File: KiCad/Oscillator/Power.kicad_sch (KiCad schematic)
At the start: 33 parts, among them SW4 SW_DPST, U10 TL074, U11 TL074, U2 TL074, U3 TL074, U4 40106, U5 TL074, U6 TL074, U7 TL074, U8 TL074, U9 TL074

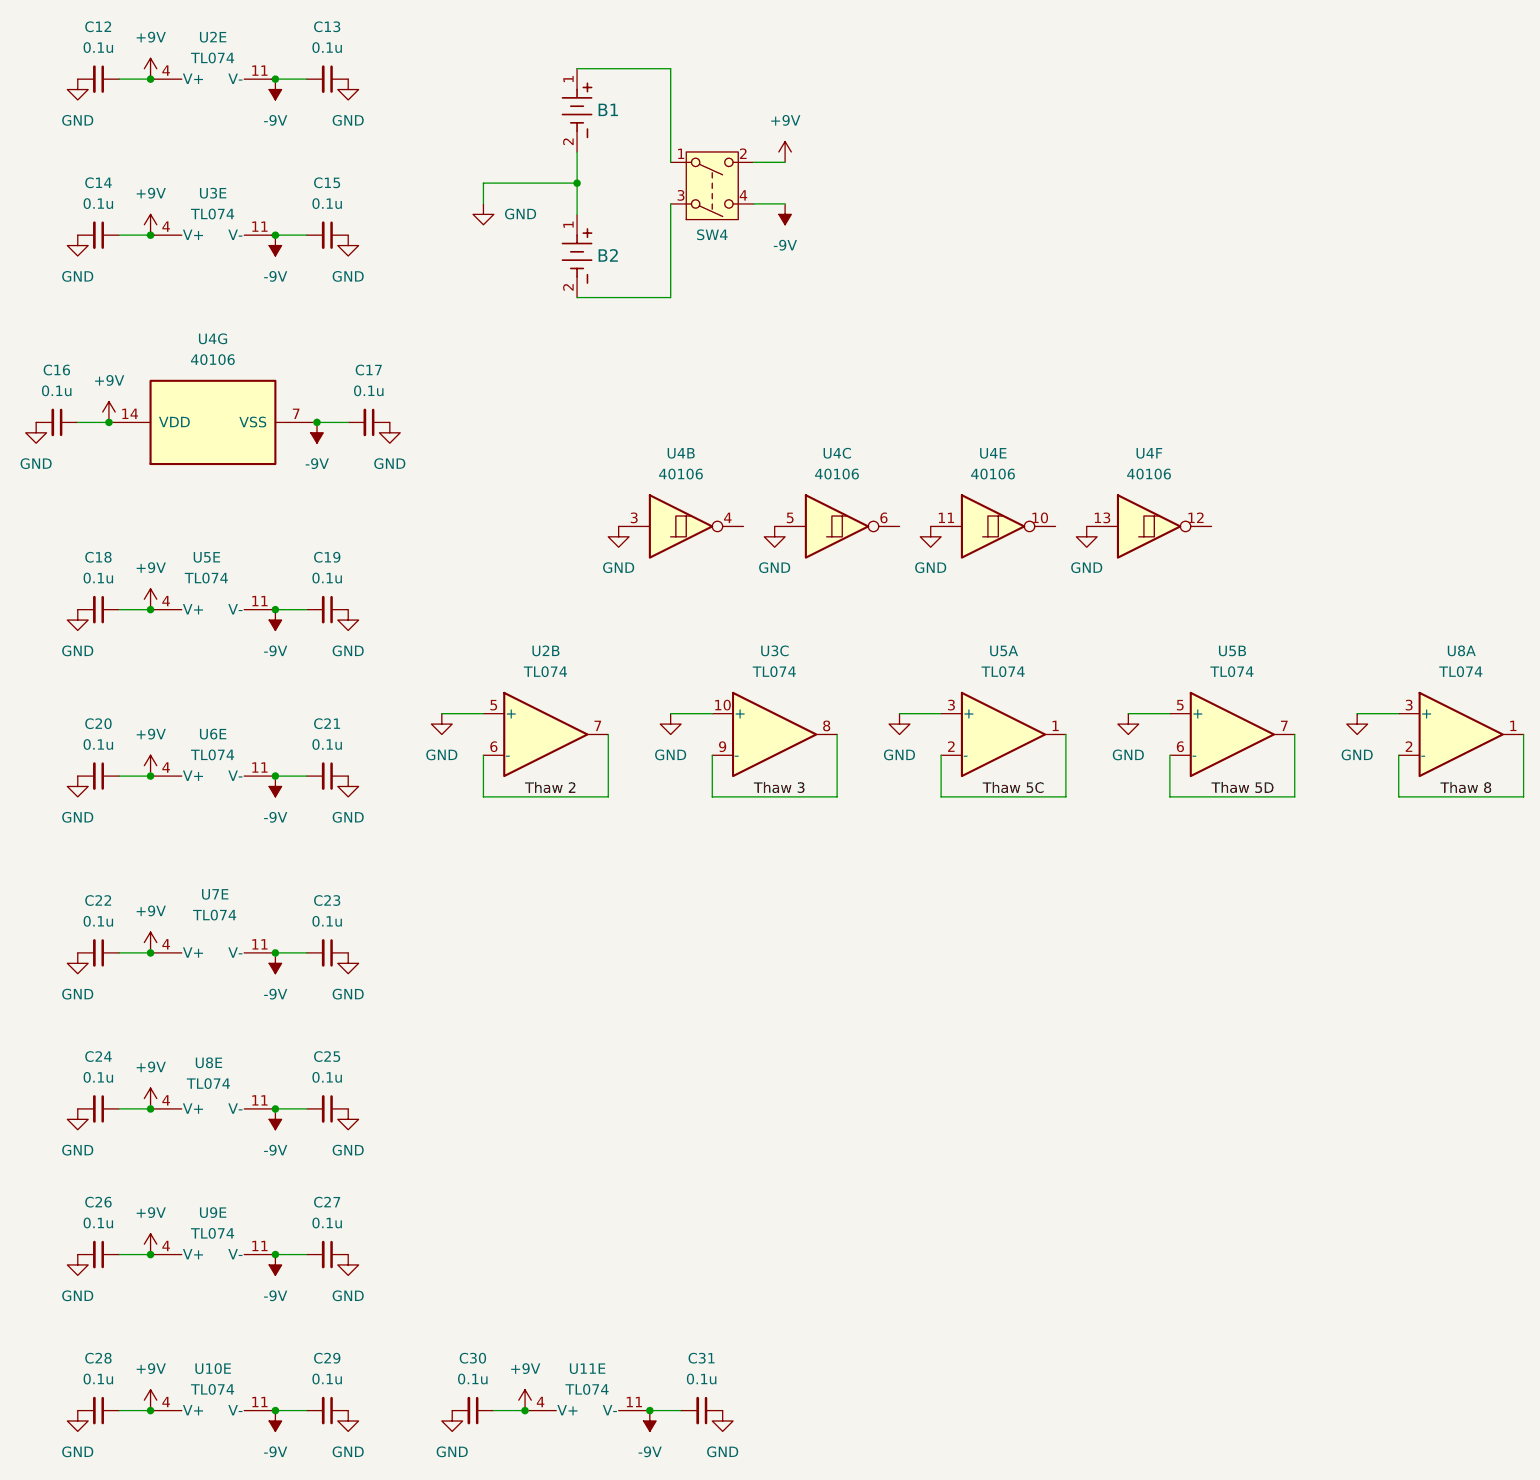
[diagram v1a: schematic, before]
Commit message: finished separating into separate kicad projects
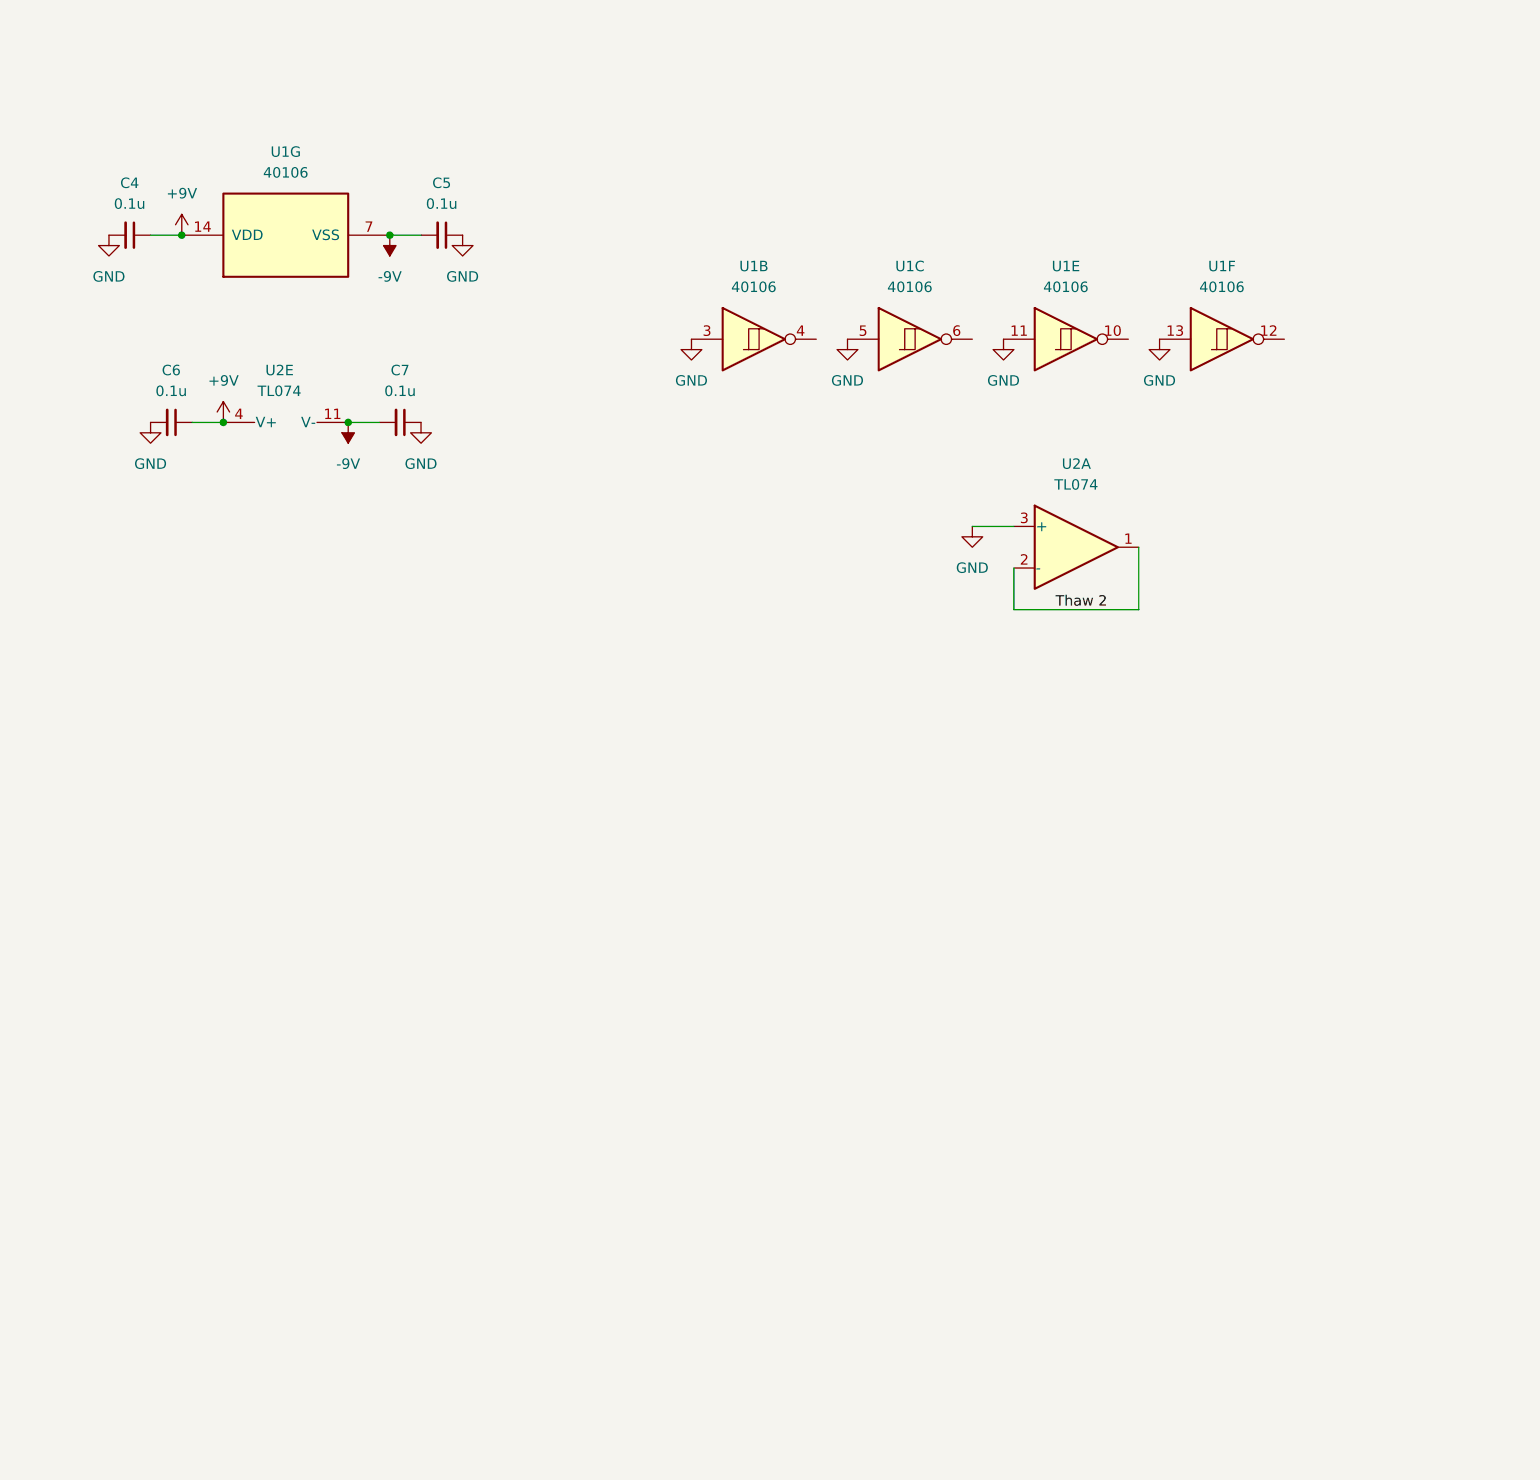
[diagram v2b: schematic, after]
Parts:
- removed B1, B2: BC9VPC, Battery Holder BC9VPC:BC9VPC_MPD, symbol 2026-06-10_00-17-41:BC9VPC
- removed C12, C13, C14, C15, C20, C21, C22, C23, C24, C25, C26, C27, C28, C29, C30, C31: 0.1u, Capacitor_SMD:C_0603_1608Metric, symbol Device:C_Small
- removed SW4: SW_DPST, DPST Switch RA83231100:DPST Switch RA83231100, symbol Switch:SW_DPST
- removed U10, U11, U2, U3, U6, U7, U8, U9: TL074, Package_DIP:DIP-14_W7.62mm, symbol Amplifier_Operational:TL074
- removed unit 2 of U5
- renumbered C16 to C4, C17 to C5, C18 to C6, C19 to C7, U4 to U1, U5 to U2
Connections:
- net Thaw 5C is gone; now on net Thaw 2: U2.1, U2.2 (-)
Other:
- moved on the sheet: C4, C5, C6, C7, U1B, U1C, U1E, U1F, U1G, U2A, U2E

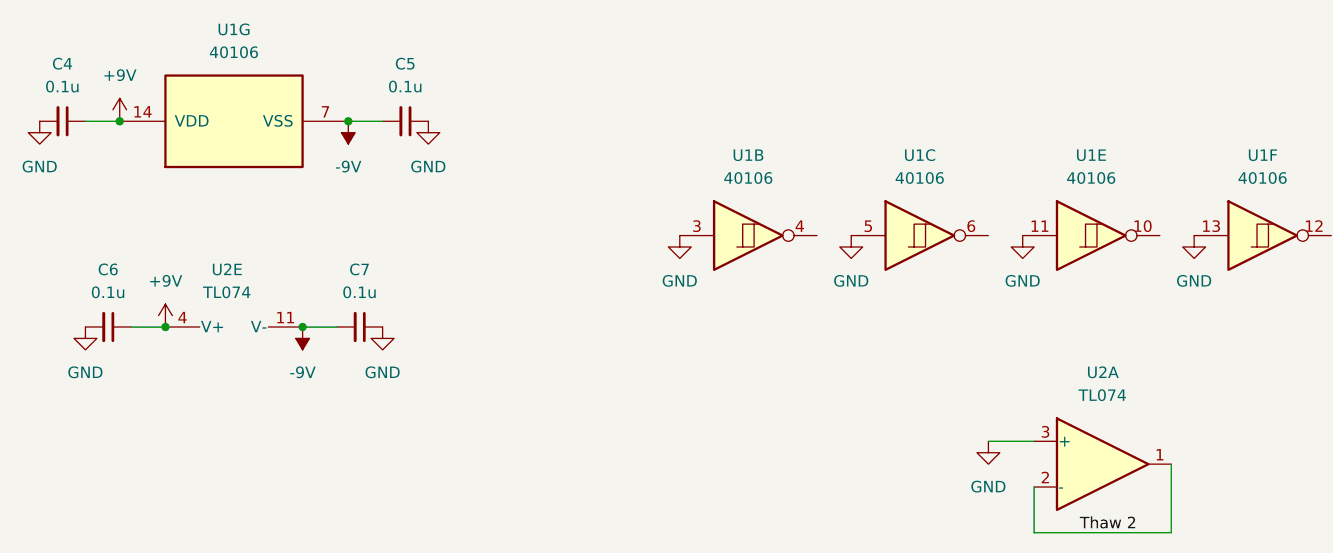
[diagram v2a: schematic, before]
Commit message: fixed critical issue in oscillator
schmitt trigger's VEE is supposed to be 0V, not -9V :wilted_rose: :wilted_rose:
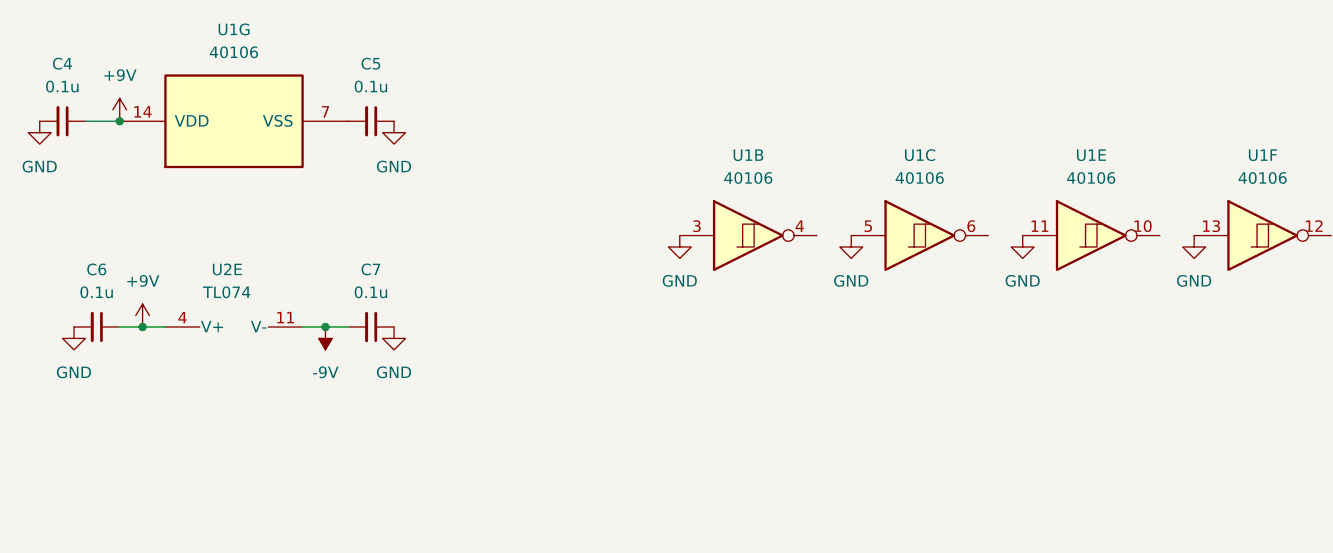
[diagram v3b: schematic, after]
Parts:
- removed unit 1 of U2
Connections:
- net -9V: no longer C5.2, U1.7 (VSS)
- new net: C5.2, U1.7 (VSS)
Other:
- moved on the sheet: C5, C6, C7

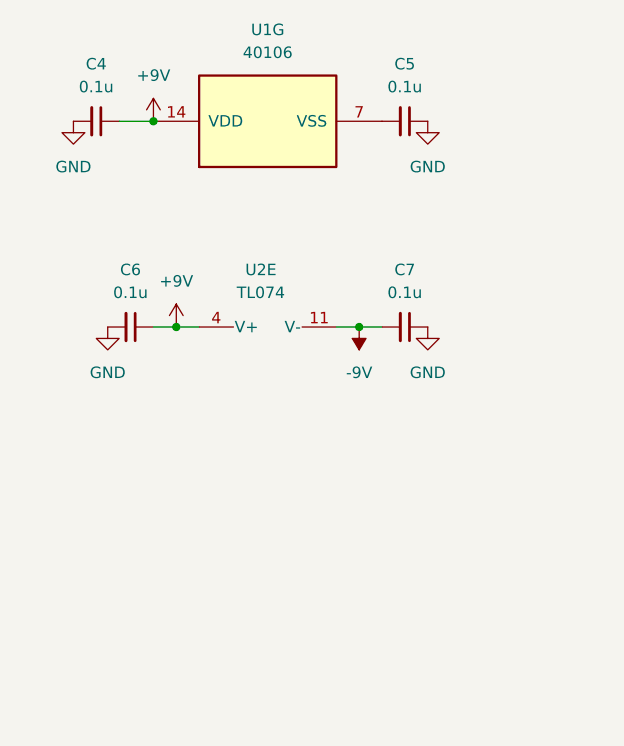
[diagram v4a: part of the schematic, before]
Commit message: added power indicator LEDs
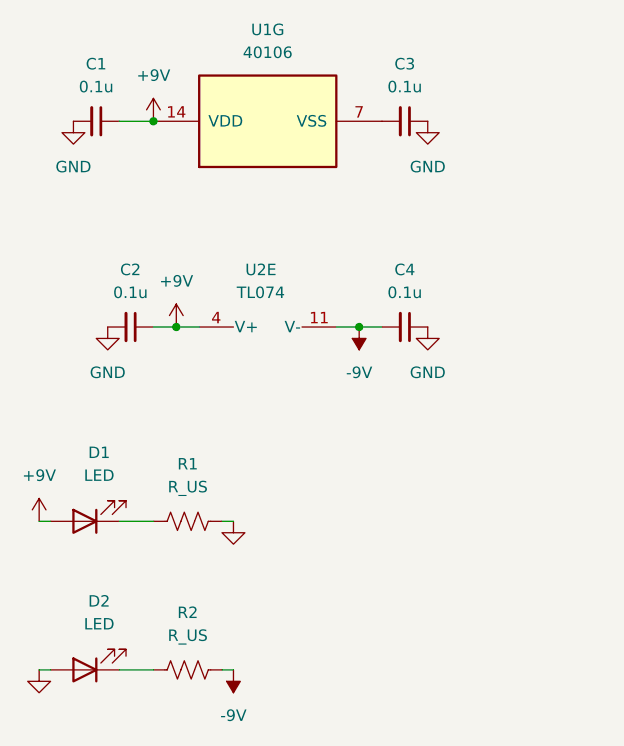
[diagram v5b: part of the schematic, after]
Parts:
- added D1, D2: LED, symbol Device:LED
- added R1, R2: R_US, symbol Device:R_US
- renumbered C4 to C1, C6 to C2, C5 to C3, C7 to C4
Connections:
- net +9V: now also D1.2 (A)
- net -9V: now also R2.2
- net GND: now also D2.2 (A), R1.2
- new net: D1.1 (K), R1.1
- new net: D2.1 (K), R2.1
